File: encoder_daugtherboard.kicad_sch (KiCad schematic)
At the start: 7 parts, among them SW7 RotaryEncoder_Switch

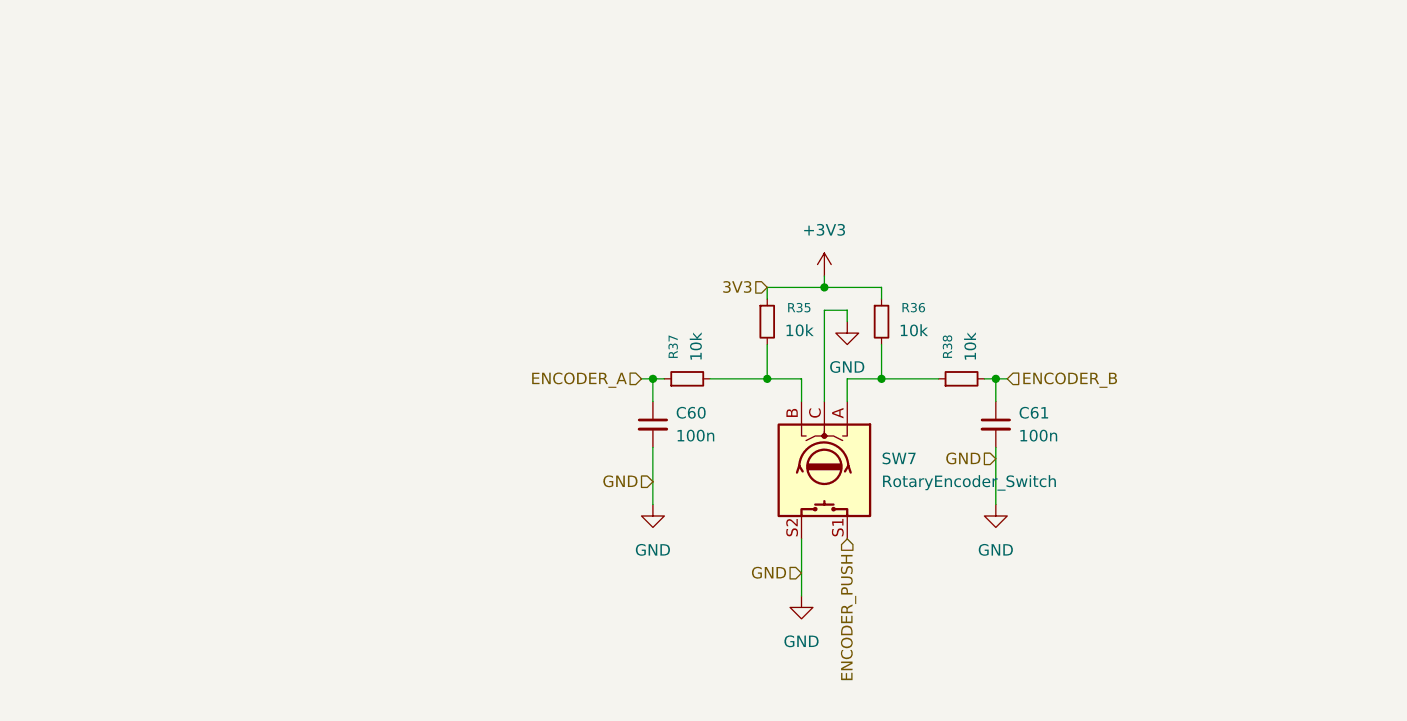
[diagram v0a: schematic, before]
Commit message: split schematic based on physical PCB split
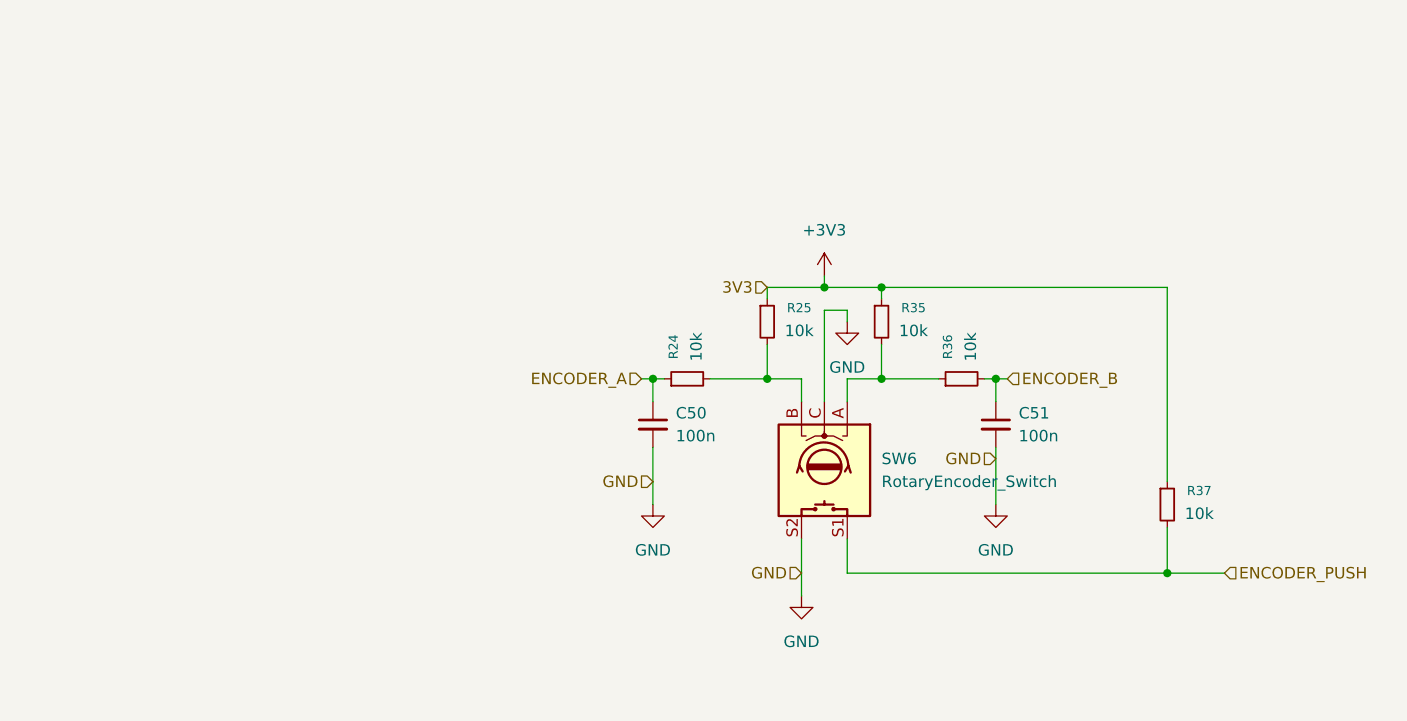
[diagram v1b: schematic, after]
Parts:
- added R37: 10k, symbol Device:R_Small
- renumbered C60 to C50, C61 to C51, R37 to R24, R35 to R25, R36 to R35, R38 to R36, SW7 to SW6
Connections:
- net +3V3: now also R37.1
- net ENCODER_PUSH: now also R37.2

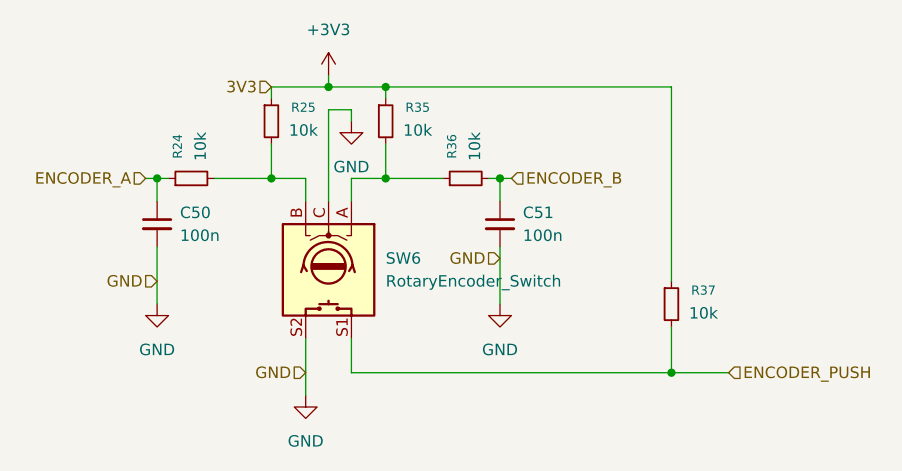
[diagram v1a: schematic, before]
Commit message: fixed page numbers
and adjusted some label types
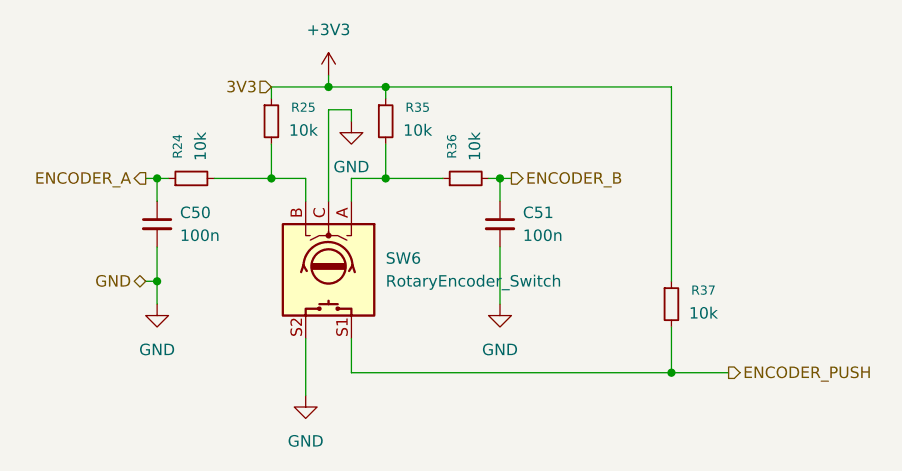
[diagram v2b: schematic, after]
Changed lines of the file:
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@@
 	(paper "A5")
 	(junction
+		(at 83.82 64.77)
+		(diameter 0)
+		(color 0 0 0 0)
+	)
+	(junction
 		(at 96.52 53.34)
 		(diameter 0)
@@
 	(wire
 		(pts
+			(xy 83.82 64.77) (xy 83.82 67.31)
+		)
+		(stroke
+			(width 0)
+			(type default)
+		)
+	)
+	(wire
+		(pts
 			(xy 105.41 53.34) (xy 109.22 53.34)
 		)
@@
 	(wire
 		(pts
-			(xy 83.82 60.96) (xy 83.82 67.31)
+			(xy 83.82 60.96) (xy 83.82 64.77)
 		)
 		(stroke
@@
 	(wire
 		(pts
+			(xy 82.55 64.77) (xy 83.82 64.77)
+		)
+		(stroke
+			(width 0)
+			(type default)
+		)
+	)
+	(wire
+		(pts
 			(xy 140.97 64.77) (xy 140.97 43.18)
 		)
@@
 	)
 	(hierarchical_label "ENCODER_A"
-		(shape input)
+		(shape output)
 		(at 82.55 53.34 180)
 		(effects
@@
 	)
 	(hierarchical_label "ENCODER_B"
-		(shape input)
+		(shape output)
 		(at 123.19 53.34 0)
 		(effects
@@
 	)
 	(hierarchical_label "GND"
-		(shape input)
-		(at 121.92 62.23 180)
+		(shape bidirectional)
+		(at 82.55 64.77 180)
 		(effects
 			(font
@@
 		)
 	)
-	(hierarchical_label "GND"
-		(shape input)
-		(at 83.82 64.77 180)
-		(effects
-			(font
-				(size 1.27 1.27)
-			)
-			(justify right)
-		)
-	)
 	(hierarchical_label "ENCODER_PUSH"
-		(shape input)
+		(shape output)
 		(at 147.32 74.93 0)
 		(effects
@@
 		)
 	)
-	(hierarchical_label "GND"
-		(shape input)
-		(at 100.33 74.93 180)
-		(effects
-			(font
-				(size 1.27 1.27)
-			)
-			(justify right)
-		)
-	)

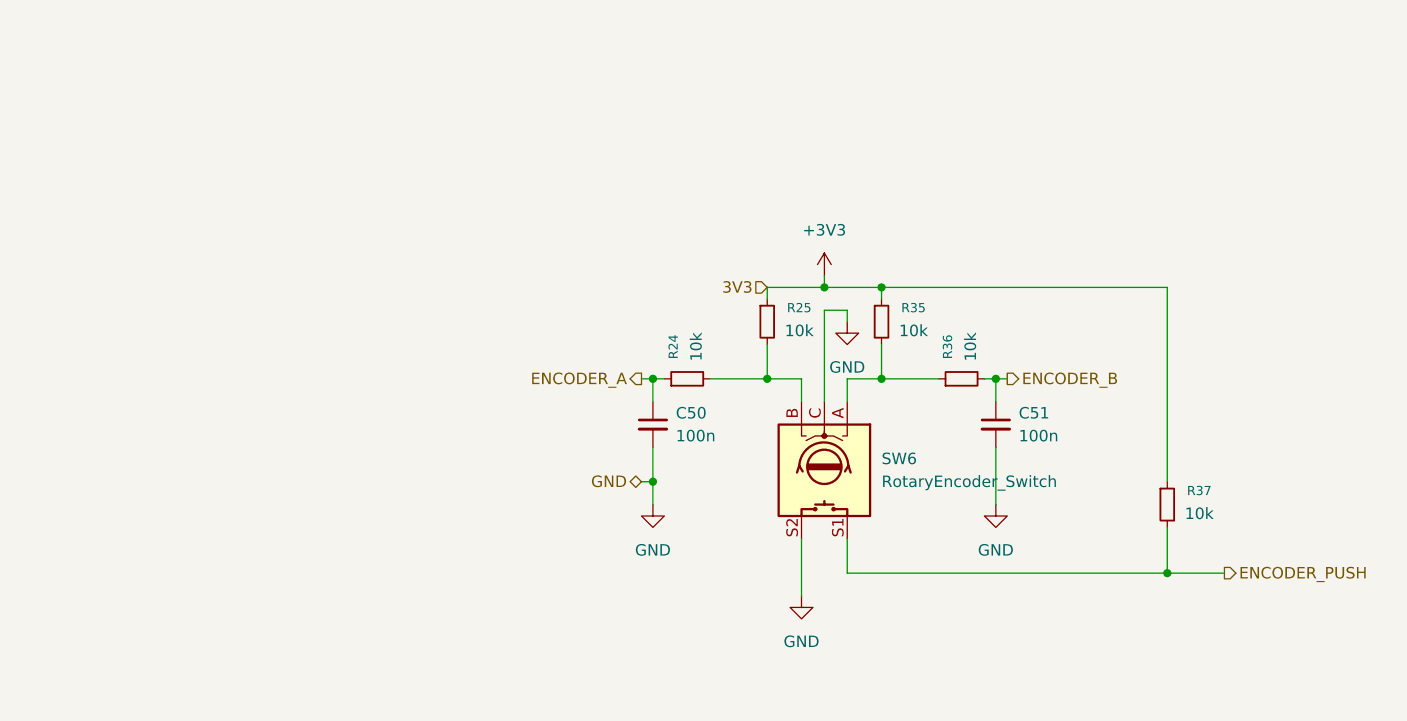
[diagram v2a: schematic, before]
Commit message: separating schematics based on board
finished splitting every component up into separate sheets in the schematic based on what physical board it's going on
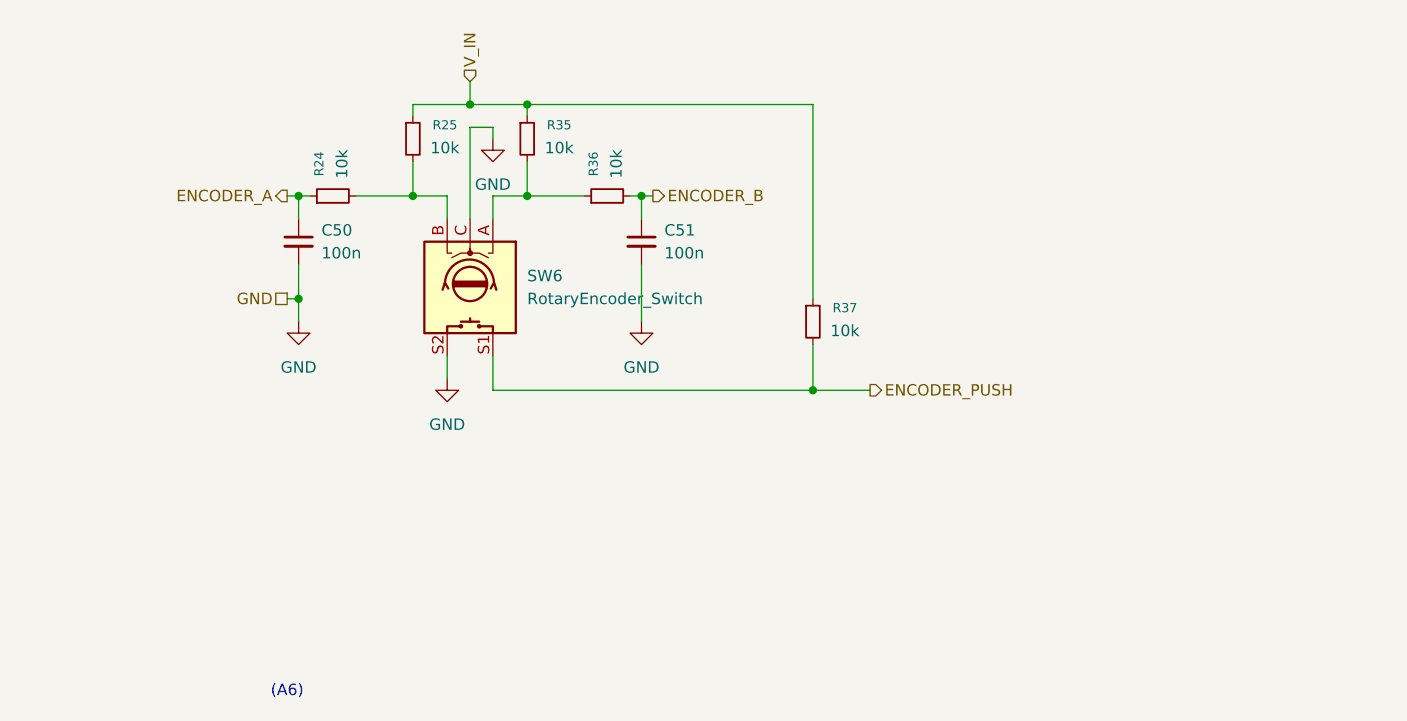
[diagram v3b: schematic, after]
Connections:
- net +3V3 renamed V_IN
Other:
- note added: "(A6)"
- moved on the sheet: C50, C51, R24, R25, R35, R36, R37, SW6

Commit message: assigning pcb footprints
assigned pcb footprints to most components:

- rotary encoder footprint will need slight modification to fit bourns PEC11L

- need to finalize components for reset button and the four switches before assigning those footprints
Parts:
- C50, C51: footprint (none) -> Capacitor_SMD:C_1206_3216Metric
- R24, R25, R35, R36, R37: footprint (none) -> Resistor_SMD:R_1206_3216Metric
- SW6: footprint (none) -> Rotary_Encoder:RotaryEncoder_Alps_EC11E-Switch_Vertical_H20mm
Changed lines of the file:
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@@
 			)
 		)
-		(property "Footprint" ""
+		(property "Footprint" "Resistor_SMD:R_1206_3216Metric"
 			(at 57.15 26.67 0)
 			(effects
@@
 			)
 		)
-		(property "Footprint" ""
+		(property "Footprint" "Rotary_Encoder:RotaryEncoder_Alps_EC11E-Switch_Vertical_H20mm"
 			(at 67.564 39.37 0)
 			(effects
@@
 			)
 		)
-		(property "Footprint" ""
+		(property "Footprint" "Resistor_SMD:R_1206_3216Metric"
 			(at 48.26 33.02 0)
 			(effects
@@
 			)
 		)
-		(property "Footprint" ""
+		(property "Footprint" "Resistor_SMD:R_1206_3216Metric"
 			(at 78.74 33.02 0)
 			(effects
@@
 			)
 		)
-		(property "Footprint" ""
+		(property "Footprint" "Resistor_SMD:R_1206_3216Metric"
 			(at 69.85 26.67 0)
 			(effects
@@
 			)
 		)
-		(property "Footprint" ""
+		(property "Footprint" "Capacitor_SMD:C_1206_3216Metric"
 			(at 82.55 38.1 0)
 			(effects
@@
 			)
 		)
-		(property "Footprint" ""
+		(property "Footprint" "Resistor_SMD:R_1206_3216Metric"
 			(at 101.6 46.99 0)
 			(effects
@@
 			)
 		)
-		(property "Footprint" ""
+		(property "Footprint" "Capacitor_SMD:C_1206_3216Metric"
 			(at 44.45 38.1 0)
 			(effects

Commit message: finalizing schematics
connected the new DAC footprint, filled in title blocks
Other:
- company: (none) -> rien+la_reine;
- title: (none) -> Tome: Encoder Daughterboard

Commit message: working on PCBs
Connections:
- net ENCODER_A: now also C51.1, R36.2; no longer C50.1, R24.1
- net ENCODER_B: now also C50.1, R24.1; no longer C51.1, R36.2
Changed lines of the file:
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@@
 		)
 	)
-	(hierarchical_label "ENCODER_A"
+	(hierarchical_label "ENCODER_B"
 		(shape output)
 		(at 43.18 33.02 180)
@@
 		)
 	)
-	(hierarchical_label "ENCODER_B"
+	(hierarchical_label "ENCODER_A"
 		(shape output)
 		(at 83.82 33.02 0)
@@
 		(on_board yes)
 		(dnp no)
-		(fields_autoplaced yes)
 		(property "Reference" "SW6"
-			(at 69.85 41.9099 90)
+			(at 69.85 41.656 0)
 			(effects
 				(font
@@
 		)
 		(property "Value" "RotaryEncoder_Switch"
-			(at 69.85 44.4499 90)
-			(effects
-				(font
+			(at 72.136 33.528 0)
+			(effects
+				(font

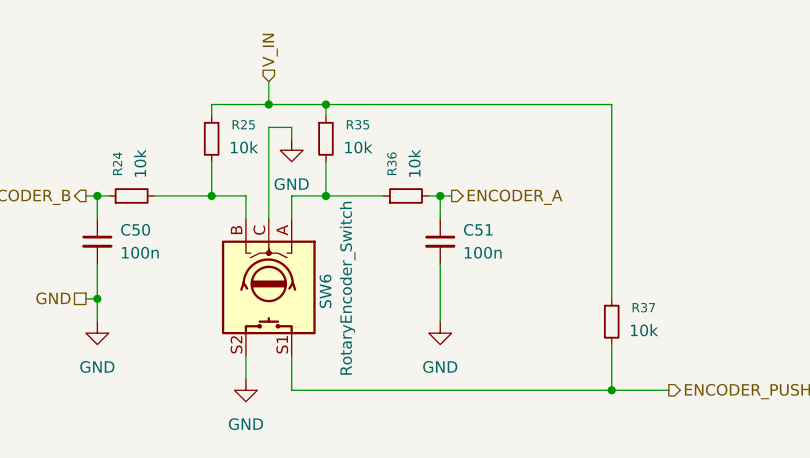
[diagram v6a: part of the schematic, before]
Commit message: different encoder board layout
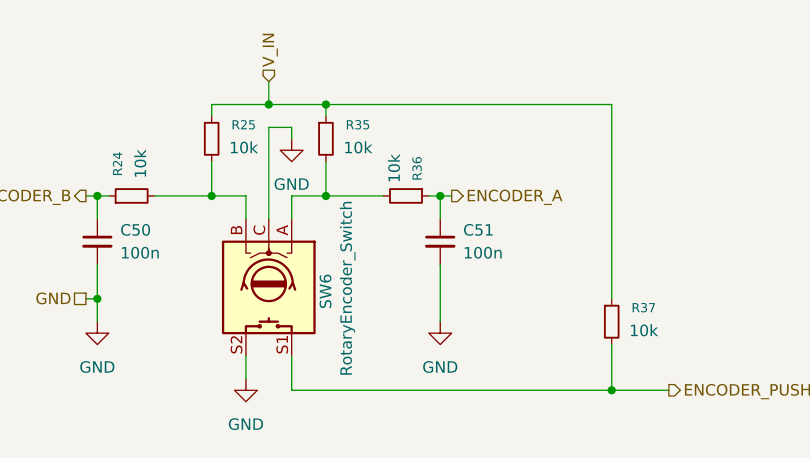
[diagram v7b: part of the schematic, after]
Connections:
- net ENCODER_A: now also R36.1; no longer R36.2
- net at R35.2, SW6.A: now also R36.2; no longer R36.1
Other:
- moved on the sheet: R36
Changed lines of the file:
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@@
 		(lib_name "R_Small_4")
 		(lib_id "Device:R_Small")
-		(at 78.74 33.02 90)
+		(at 78.74 33.02 270)
 		(unit 1)
 		(exclude_from_sim no)
@@
 		(dnp no)
 		(property "Reference" "R36"
-			(at 77.216 29.464 0)
+			(at 80.01 29.972 0)
 			(effects
 				(font
@@
 		)
 		(property "Value" "10k"
-			(at 79.756 29.464 0)
+			(at 77.47 29.972 0)
 			(effects
 				(font

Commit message: workshopping encoder board
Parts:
- added J10, J12, J14, J16: Conn_01x02_Pin, Connector_PinHeader_2.00mm:PinHeader_1x02_P2.00mm_Vertical, symbol Connector:Conn_01x02_Pin
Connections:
- net ENCODER_A: now also J10.1 (Pin_1)
- net ENCODER_B: now also J10.2 (Pin_2)
- net ENCODER_PUSH: now also J12.2 (Pin_2)
- net GND: now also J14.1 (Pin_1), J14.2 (Pin_2), J16.1 (Pin_1), J16.2 (Pin_2)
- net V_IN: now also J12.1 (Pin_1)
